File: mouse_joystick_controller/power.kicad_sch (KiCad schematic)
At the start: 3 parts

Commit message: Add power jack
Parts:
- added P1: PWR_JACK_2.1x5.5_SMD_RA, Janelia:DCJACK_3PAD_SMD_RA, symbol Janelia:PWR_JACK_2.1x5.5_SMD_RA
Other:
- company: (none) -> Howard Hughes Medical Institute
- title: (none) -> mouse_joystick_controller
- moved on the sheet: C6, C7, REG1

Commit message: Modify brake
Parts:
- renumbered P1 to P?
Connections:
- net +24V: now also P?.1 (P1)
- net GND: now also P?.2 (P2)
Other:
- moved on the sheet: P?
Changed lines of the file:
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@@
+    (stroke (width 0) (type default))
+  )
+  (wire (pts (xy 110.49 62.23) (xy 107.95 62.23))
     (stroke (width 0) (type default))
   )
@@
     (stroke (width 0) (type default))
   )
-  (wire (pts (xy 83.82 104.14) (xy 81.28 104.14))
-    (stroke (width 0) (type default))
-  )
   (wire (pts (xy 135.89 88.9) (xy 135.89 91.44))
     (stroke (width 0) (type default))
@@
     (stroke (width 0) (type default))
   )
+  (wire (pts (xy 110.49 64.77) (xy 107.95 64.77))
+    (stroke (width 0) (type default))
+  )
   (wire (pts (xy 148.59 93.98) (xy 151.13 93.98))
     (stroke (width 0) (type default))
@@
     (effects (font (size 1.27 1.27)) (justify left bottom))
   )
+  (label "+24V" (at 110.49 64.77 0) (fields_autoplaced)
+    (effects (font (size 1.27 1.27)) (justify left bottom))
+  )
+  (label "GND" (at 110.49 62.23 0) (fields_autoplaced)
+    (effects (font (size 1.27 1.27)) (justify left bottom))
+  )
   (label "GND" (at 195.58 104.14 270) (fields_autoplaced)
     (effects (font (size 1.27 1.27)) (justify right bottom))
@@
     (effects (font (size 1.27 1.27)) (justify left bottom))
   )
-  (label "POWER_ENABLE" (at 83.82 105.41 0) (fields_autoplaced)
-    (effects (font (size 1.27 1.27)) (justify left bottom))
-  )
   (hierarchical_label "GND" (shape passive) (at 81.28 100.33 180) (fields_autoplaced)
-    (effects (font (size 1.27 1.27)) (justify right))
-  )
-  (hierarchical_label "POWER_ENABLE" (shape input) (at 81.28 104.14 180) (fields_autoplaced)
     (effects (font (size 1.27 1.27)) (justify right))
   )
@@
     )
   )
-  (symbol (lib_id "Janelia:PWR_JACK_2.1x5.5_SMD_RA") (at 119.38 58.42 0) (unit 1)
+  (symbol (lib_id "Janelia:PWR_JACK_2.1x5.5_SMD_RA") (at 102.87 63.5 180) (unit 1)
     (in_bom yes) (on_board yes) (dnp no) (fields_autoplaced)
-    (property "Reference" "P1" (at 121.92 57.785 0)
-      (effects (font (size 1.27 1.27)) (justify left))
-    )
-    (property "Value" "PWR_JACK_2.1x5.5_SMD_RA" (at 121.92 60.325 0)
-      (effects (font (size 1.27 1.27)) (justify left))
-    )
-    (property "Footprint" "Janelia:DCJACK_3PAD_SMD_RA" (at 116.84 57.15 0)
-      (effects (font (size 1.524 1.524)) hide)
-    )
-    (property "Datasheet" "" (at 119.38 54.61 0)
+    (property "Reference" "P?" (at 102.87 59.69 0)
+      (effects (font (size 1.27 1.27)))
+    )
+    (property "Value" "PWR_JACK_2.1x5.5_SMD_RA" (at 100.33 63.5 90)
+      (effects (font (size 1.27 1.27)) hide)
+    )
+    (property "Footprint" "Janelia:DCJACK_3PAD_SMD_RA" (at 105.41 64.77 0)
+      (effects (font (size 1.524 1.524)) hide)
+    )
+    (property "Datasheet" "" (at 102.87 67.31 0)
       (effects (font (size 1.524 1.524)))
     )
-    (property "Vendor" "Digi-Key" (at 121.92 52.07 0)
-      (effects (font (size 1.524 1.524)) hide)
-    )
-    (property "Vendor Part Number" "CP-036AHPJCT-ND" (at 124.46 49.53 0)
-      (effects (font (size 1.524 1.524)) hide)
-    )
-    (property "Description" "CONN PWR JACK 2X5.5MM SOLDER" (at 127 46.99 0)
-      (effects (font (size 1.524 1.524)) hide)
-    )
-    (property "Manufacturer" "CUI Devices" (at 119.38 58.42 0)
+    (property "Vendor" "Digi-Key" (at 100.33 69.85 0)
+      (effects (font (size 1.524 1.524)) hide)
+    )
+    (property "Vendor Part Number" "CP-036AHPJCT-ND" (at 97.79 72.39 0)
+      (effects (font (size 1.524 1.524)) hide)
+    )
+    (property "Description" "CONN PWR JACK 2X5.5MM SOLDER" (at 95.25 74.93 0)
+      (effects (font (size 1.524 1.524)) hide)
+    )
+    (property "Manufacturer" "CUI Devices" (at 102.87 63.5 0)
       (effects (font (size 1.27 1.27)) hide)
     )
-    (property "Manufacturer Part Number" "PJ-036AH-SMT-TR" (at 119.38 58.42 0)
+    (property "Manufacturer Part Number" "PJ-036AH-SMT-TR" (at 102.87 63.5 0)
       (effects (font (size 1.27 1.27)) hide)
     )
@@
       (project "mouse_joystick_controller"
         (path "/cc457ebc-4af6-4663-b19f-8cb38f061cb4/f62b8726-10b6-4dce-a8d7-bdccf22557c3"
-          (reference "P1") (unit 1)
+          (reference "P?") (unit 1)
         )
       )

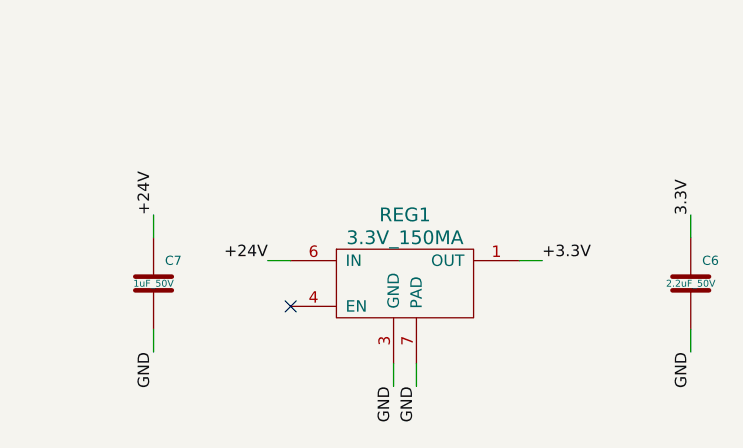
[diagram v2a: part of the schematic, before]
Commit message: Add encoder, lickport, and torque_sensor sheets
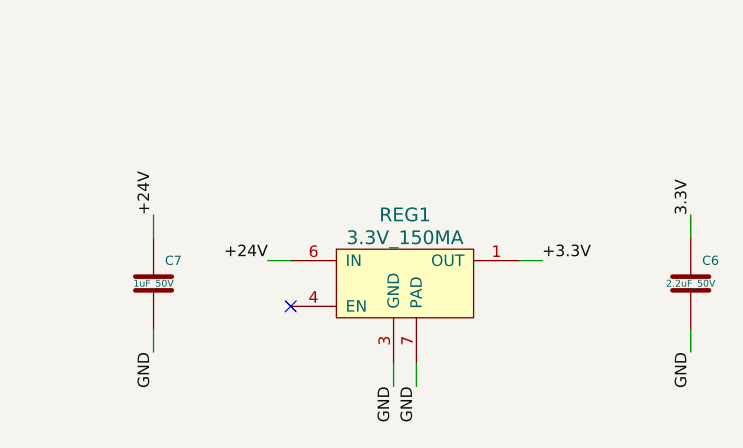
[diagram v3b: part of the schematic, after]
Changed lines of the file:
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@@
   (title_block
     (title "mouse_joystick_controller")
-    (date "2023-05-18")
+    (date "2023-05-22")
     (rev "2.0")
     (company "Howard Hughes Medical Institute")

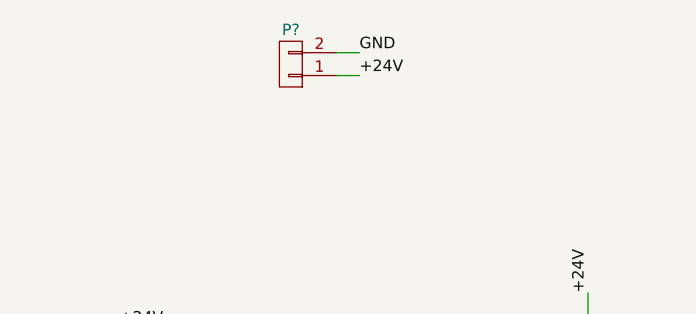
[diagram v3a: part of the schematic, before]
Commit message: Rearrange sheets
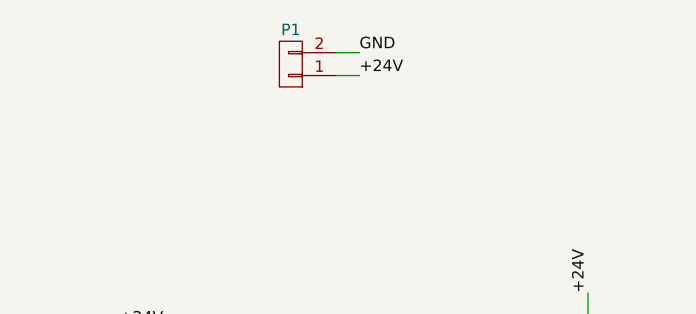
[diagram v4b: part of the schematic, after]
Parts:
- gave numbers to parts that had none: 1
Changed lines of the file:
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@@
   (title_block
     (title "mouse_joystick_controller")
-    (date "2023-05-22")
+    (date "2023-05-24")
     (rev "2.0")
     (company "Howard Hughes Medical Institute")
@@
         )
         (path "/cc457ebc-4af6-4663-b19f-8cb38f061cb4/f62b8726-10b6-4dce-a8d7-bdccf22557c3"
-          (reference "C4") (unit 1)
+          (reference "C2") (unit 1)
         )
       )
@@
         )
         (path "/cc457ebc-4af6-4663-b19f-8cb38f061cb4/f62b8726-10b6-4dce-a8d7-bdccf22557c3"
-          (reference "C3") (unit 1)
+          (reference "C1") (unit 1)
         )
       )
@@
   (symbol (lib_id "Janelia:PWR_JACK_2.1x5.5_SMD_RA") (at 102.87 63.5 180) (unit 1)
     (in_bom yes) (on_board yes) (dnp no) (fields_autoplaced)
-    (property "Reference" "P?" (at 102.87 59.69 0)
+    (property "Reference" "P1" (at 102.87 59.69 0)
       (effects (font (size 1.27 1.27)))
     )
@@
       (project "mouse_joystick_controller"
         (path "/cc457ebc-4af6-4663-b19f-8cb38f061cb4/f62b8726-10b6-4dce-a8d7-bdccf22557c3"
-          (reference "P?") (unit 1)
+          (reference "P1") (unit 1)
         )
       )

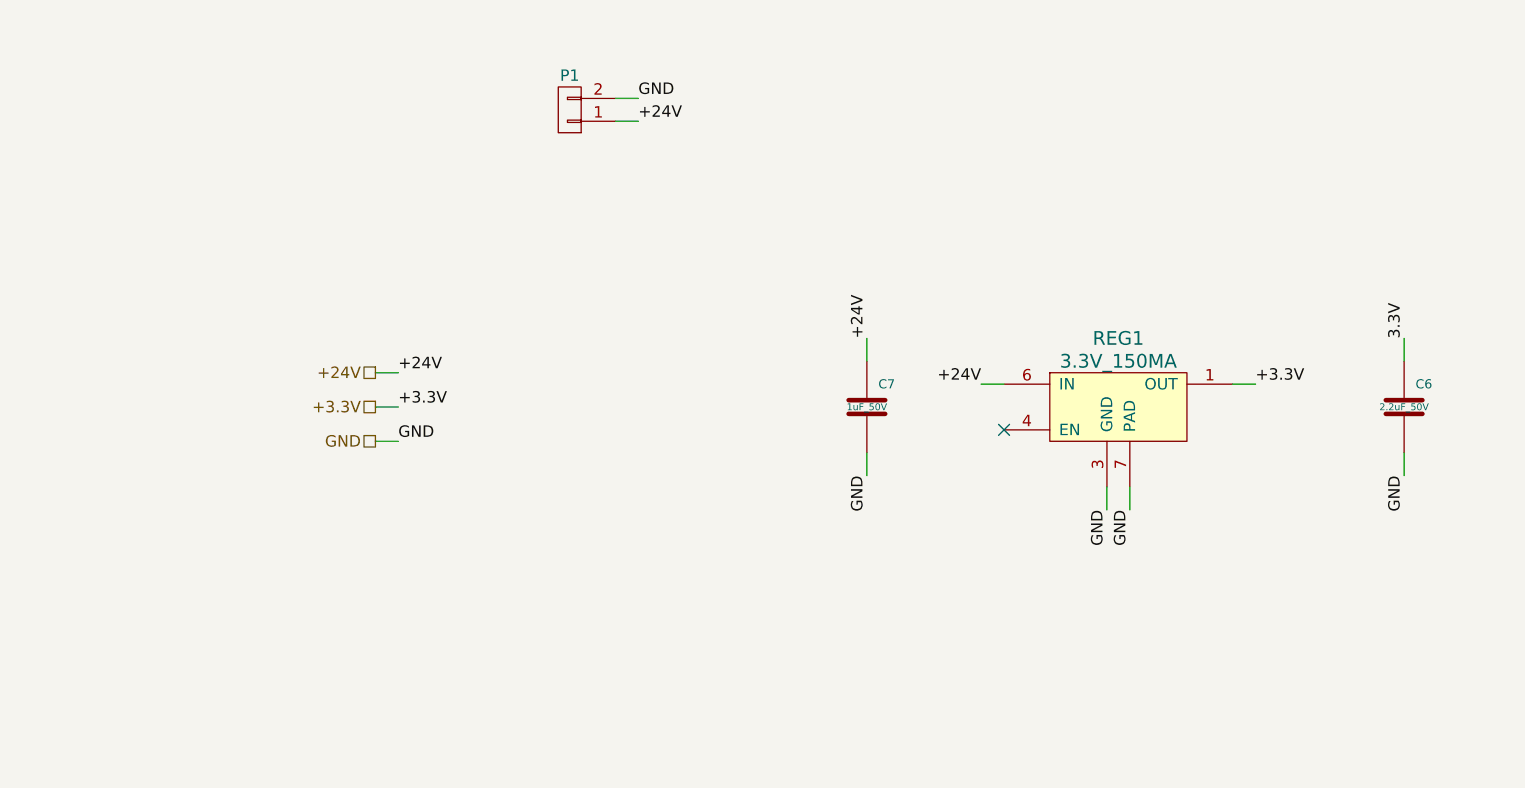
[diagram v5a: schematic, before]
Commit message: Add barrel jack connectors
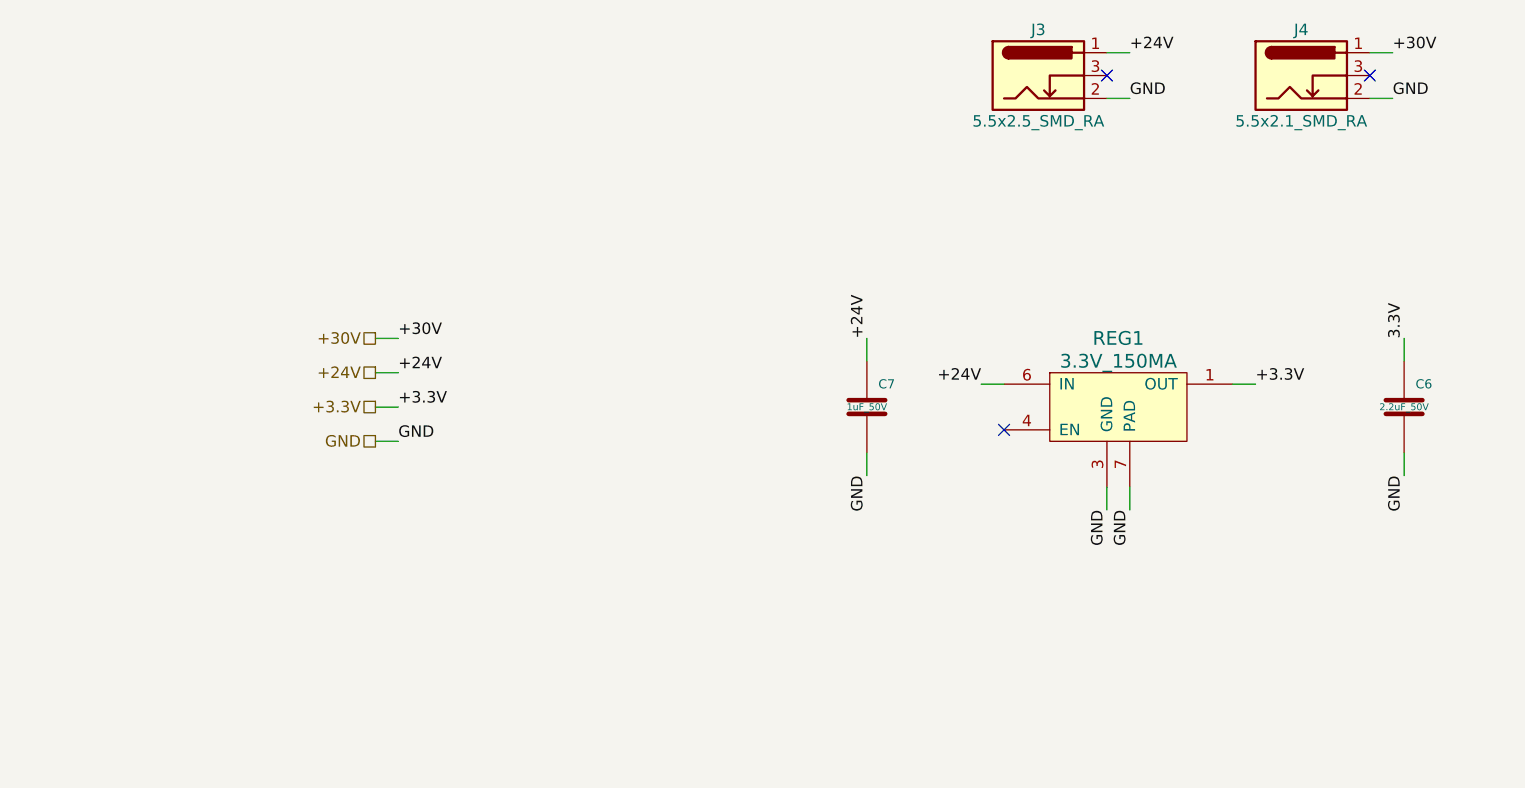
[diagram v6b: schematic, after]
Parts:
- removed P1: PWR_JACK_2.1x5.5_SMD_RA, Janelia:DCJACK_3PAD_SMD_RA, symbol Janelia:PWR_JACK_2.1x5.5_SMD_RA
- added J3: 5.5x2.5_SMD_RA, Janelia:CONN_54-00165, symbol Janelia:Barrel_Jack_Switch_5.5x2.5_SMD_RA_54-00165
- added J4: 5.5x2.1_SMD_RA, Janelia:CONN_54-00164, symbol Janelia:Barrel_Jack_Switch_5.5x2.1_SMD_RA_54-00164
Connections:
- net +24V: now also J3.1
- net GND: now also J3.2, J4.2
- new net +30V: J4.1
- no-connect marks 1 -> 3
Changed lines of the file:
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@@
     (company "Howard Hughes Medical Institute")
   )
+  (no_connect (at 162.56 59.69))
   (no_connect (at 151.13 99.06))
+  (no_connect (at 191.77 59.69))
   (wire (pts (xy 195.58 91.44) (xy 195.58 88.9))
     (stroke (width 0) (type default))
@@
     (stroke (width 0) (type default))
   )
+  (wire (pts (xy 194.31 57.15) (xy 191.77 57.15))
+    (stroke (width 0) (type default))
+  )
   (wire (pts (xy 195.58 101.6) (xy 195.58 104.14))
     (stroke (width 0) (type default))
@@
     (stroke (width 0) (type default))
   )
-  (wire (pts (xy 110.49 62.23) (xy 107.95 62.23))
+  (wire (pts (xy 194.31 62.23) (xy 191.77 62.23))
+    (stroke (width 0) (type default))
+  )
+  (wire (pts (xy 165.1 62.23) (xy 162.56 62.23))
     (stroke (width 0) (type default))
   )
@@
     (stroke (width 0) (type default))
   )
+  (wire (pts (xy 83.82 88.9) (xy 81.28 88.9))
+    (stroke (width 0) (type default))
+  )
   (wire (pts (xy 83.82 92.71) (xy 81.28 92.71))
     (stroke (width 0) (type default))
@@
     (stroke (width 0) (type default))
   )
-  (wire (pts (xy 110.49 64.77) (xy 107.95 64.77))
+  (wire (pts (xy 165.1 57.15) (xy 162.56 57.15))
     (stroke (width 0) (type default))
   )
@@
     (effects (font (size 1.27 1.27)) (justify right bottom))
   )
+  (label "+30V" (at 83.82 88.9 0) (fields_autoplaced)
+    (effects (font (size 1.27 1.27)) (justify left bottom))
+  )
   (label "+24V" (at 148.59 93.98 180) (fields_autoplaced)
     (effects (font (size 1.27 1.27)) (justify right bottom))
@@
     (effects (font (size 1.27 1.27)) (justify left bottom))
   )
-  (label "+24V" (at 110.49 64.77 0) (fields_autoplaced)
-    (effects (font (size 1.27 1.27)) (justify left bottom))
-  )
-  (label "GND" (at 110.49 62.23 0) (fields_autoplaced)
+  (label "+24V" (at 165.1 57.15 0) (fields_autoplaced)
+    (effects (font (size 1.27 1.27)) (justify left bottom))
+  )
+  (label "GND" (at 165.1 62.23 0) (fields_autoplaced)
     (effects (font (size 1.27 1.27)) (justify left bottom))
   )
@@
     (effects (font (size 1.27 1.27)) (justify left bottom))
   )
+  (label "GND" (at 194.31 62.23 0) (fields_autoplaced)
+    (effects (font (size 1.27 1.27)) (justify left bottom))
+  )
   (label "+3.3V" (at 83.82 96.52 0) (fields_autoplaced)
     (effects (font (size 1.27 1.27)) (justify left bottom))
@@
     (effects (font (size 1.27 1.27)) (justify left bottom))
   )
+  (label "+30V" (at 194.31 57.15 0) (fields_autoplaced)
+    (effects (font (size 1.27 1.27)) (justify left bottom))
+  )
   (hierarchical_label "GND" (shape passive) (at 81.28 100.33 180) (fields_autoplaced)
+    (effects (font (size 1.27 1.27)) (justify right))
+  )
+  (hierarchical_label "+30V" (shape passive) (at 81.28 88.9 180) (fields_autoplaced)
     (effects (font (size 1.27 1.27)) (justify right))
   )
@@
     )
   )
+  (symbol (lib_id "Janelia:Barrel_Jack_Switch_5.5x2.5_SMD_RA_54-00165") (at 154.94 59.69 0) (unit 1)
+    (in_bom yes) (on_board yes) (dnp no)
+    (property "Reference" "J3" (at 154.94 54.61 0)
+      (effects (font (size 1.27 1.27)))
+    )
+    (property "Value" "5.5x2.5_SMD_RA" (at 154.94 64.77 0)
+      (effects (font (size 1.27 1.27)))
+    )
+    (property "Footprint" "Janelia:CONN_54-00165" (at 154.94 48.895 0)
+      (effects (font (size 1.524 1.524)) hide)
+    )
+    (property "Datasheet" "" (at 154.94 55.88 0)
+      (effects (font (size 1.524 1.524)))
+    )
+    (property "Vendor" "Digi-Key" (at 154.94 45.72 0)
+      (effects (font (size 1.524 1.524)) hide)
+    )
+    (property "Vendor Part Number" "839-54-00165CT-ND" (at 154.94 43.18 0)
+      (effects (font (size 1.524 1.524)) hide)
+    )
+    (property "Description" "CONN JACK R/A SMT 5.5X2.5MM" (at 154.94 40.005 0)
+      (effects (font (size 1.524 1.524)) hide)
+    )
+    (property "Manufacturer" "Tensility International Corp" (at 154.94 52.07 0)
+      (effects (font (size 1.27 1.27)) hide)
+    )
+    (property "Manufacturer Part Number" "54-00165" (at 155.575 37.465 0)
+      (effects (font (size 1.27 1.27)) hide)
+    )
+    (pin "1")
+    (pin "2")
+    (pin "3")
+    (instances
+      (project "mouse_joystick_controller"
+        (path "/cc457ebc-4af6-4663-b19f-8cb38f061cb4/f62b8726-10b6-4dce-a8d7-bdccf22557c3"
+          (reference "J3") (unit 1)
+        )
+      )
+    )
+  )
   (symbol (lib_id "Janelia:C_1uF_50V_0603") (at 135.89 96.52 0) (unit 1)
     (in_bom yes) (on_board yes) (dnp no)
@@
     )
   )
-  (symbol (lib_id "Janelia:PWR_JACK_2.1x5.5_SMD_RA") (at 102.87 63.5 180) (unit 1)
-    (in_bom yes) (on_board yes) (dnp no) (fields_autoplaced)
-    (property "Reference" "P1" (at 102.87 59.69 0)
-      (effects (font (size 1.27 1.27)))
-    )
-    (property "Value" "PWR_JACK_2.1x5.5_SMD_RA" (at 100.33 63.5 90)
-      (effects (font (size 1.27 1.27)) hide)
-    )
-    (property "Footprint" "Janelia:DCJACK_3PAD_SMD_RA" (at 105.41 64.77 0)
-      (effects (font (size 1.524 1.524)) hide)
-    )
-    (property "Datasheet" "" (at 102.87 67.31 0)
-      (effects (font (size 1.524 1.524)))
-    )
-    (property "Vendor" "Digi-Key" (at 100.33 69.85 0)
-      (effects (font (size 1.524 1.524)) hide)
-    )
-    (property "Vendor Part Number" "CP-036AHPJCT-ND" (at 97.79 72.39 0)
-      (effects (font (size 1.524 1.524)) hide)
-    )
-    (property "Description" "CONN PWR JACK 2X5.5MM SOLDER" (at 95.25 74.93 0)
-      (effects (font (size 1.524 1.524)) hide)
-    )
-    (property "Manufacturer" "CUI Devices" (at 102.87 63.5 0)
-      (effects (font (size 1.27 1.27)) hide)
-    )
-    (property "Manufacturer Part Number" "PJ-036AH-SMT-TR" (at 102.87 63.5 0)
-      (effects (font (size 1.27 1.27)) hide)
-    )
-    (pin "1")
-    (pin "2")
-    (instances
-      (project "mouse_joystick_controller"
-        (path "/cc457ebc-4af6-4663-b19f-8cb38f061cb4/f62b8726-10b6-4dce-a8d7-bdccf22557c3"
-          (reference "P1") (unit 1)
-        )
-      )
-    )
-  )
   (symbol (lib_id "Janelia:CONV_DC_DC_3.3V_150MA") (at 163.83 93.98 0) (unit 1)
     (in_bom yes) (on_board yes) (dnp no) (fields_autoplaced)
@@
         )
       )
+    )
+  )
+  (symbol (lib_id "Janelia:Barrel_Jack_Switch_5.5x2.1_SMD_RA_54-00164") (at 184.15 59.69 0) (unit 1)
+    (in_bom yes) (on_board yes) (dnp no)
+    (property "Reference" "J4" (at 184.15 54.61 0)
+      (effects (font (size 1.27 1.27)))
+    )
+    (property "Value" "5.5x2.1_SMD_RA" (at 184.15 64.77 0)
+      (effects (font (size 1.27 1.27)))
+    )
+    (property "Footprint" "Janelia:CONN_54-00164" (at 184.15 48.895 0)
+      (effects (font (size 1.524 1.524)) hide)
+    )
+    (property "Datasheet" "" (at 184.15 55.88 0)
+      (effects (font (size 1.524 1.524)))
+    )
+    (property "Vendor" "Digi-Key" (at 184.15 45.72 0)
+      (effects (font (size 1.524 1.524)) hide)
+    )
+    (property "Vendor Part Number" "839-54-00164CT-ND" (at 184.15 43.18 0)
+      (effects (font (size 1.524 1.524)) hide)
+    )
+    (property "Description" "CONN JACK R/A SMT 5.5X2.1MM" (at 184.15 40.005 0)
+      (effects (font (size 1.524 1.524)) hide)
+    )
+    (property "Manufacturer" "Tensility International Corp" (at 184.15 52.07 0)
+      (effects (font (size 1.27 1.27)) hide)
+    )
+    (property "Manufacturer Part Number" "54-00164" (at 184.785 37.465 0)
+      (effects (font (size 1.27 1.27)) hide)
+    )
+    (pin "1")
+    (pin "2")
+    (pin "3")
+    (instances
+      (project "mouse_joystick_controller"
+        (path "/cc457ebc-4af6-4663-b19f-8cb38f061cb4/f62b8726-10b6-4dce-a8d7-bdccf22557c3"
+          (reference "J4") (unit 1)
+        )
+      )
